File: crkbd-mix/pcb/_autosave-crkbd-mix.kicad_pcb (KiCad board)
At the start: 2 copper layers, 133.8 x 92.2 mm, 70 parts, among them J1 MJ-4PP-9, J2 OLED, P1 i2c-pin, P2 i2c-pin, SW1 SW_PUSH, SW10 SW_PUSH, SW11 SW_PUSH, SW12 SW_PUSH, SW13 SW_PUSH, SW14 SW_PUSH, SW15 SW_PUSH, SW16 SW_PUSH, SW17 SW_PUSH, SW18 SW_PUSH, SW19 SW_PUSH, SW2 SW_PUSH, SW20 SW_PUSH, SW21 SW_PUSH, SW3 SW_PUSH, SW4 SW_PUSH, SW5 SW_PUSH, SW6 SW_PUSH, SW7 SW_PUSH, SW8 SW_PUSH, SW9 SW_PUSH, U1 ProMicro

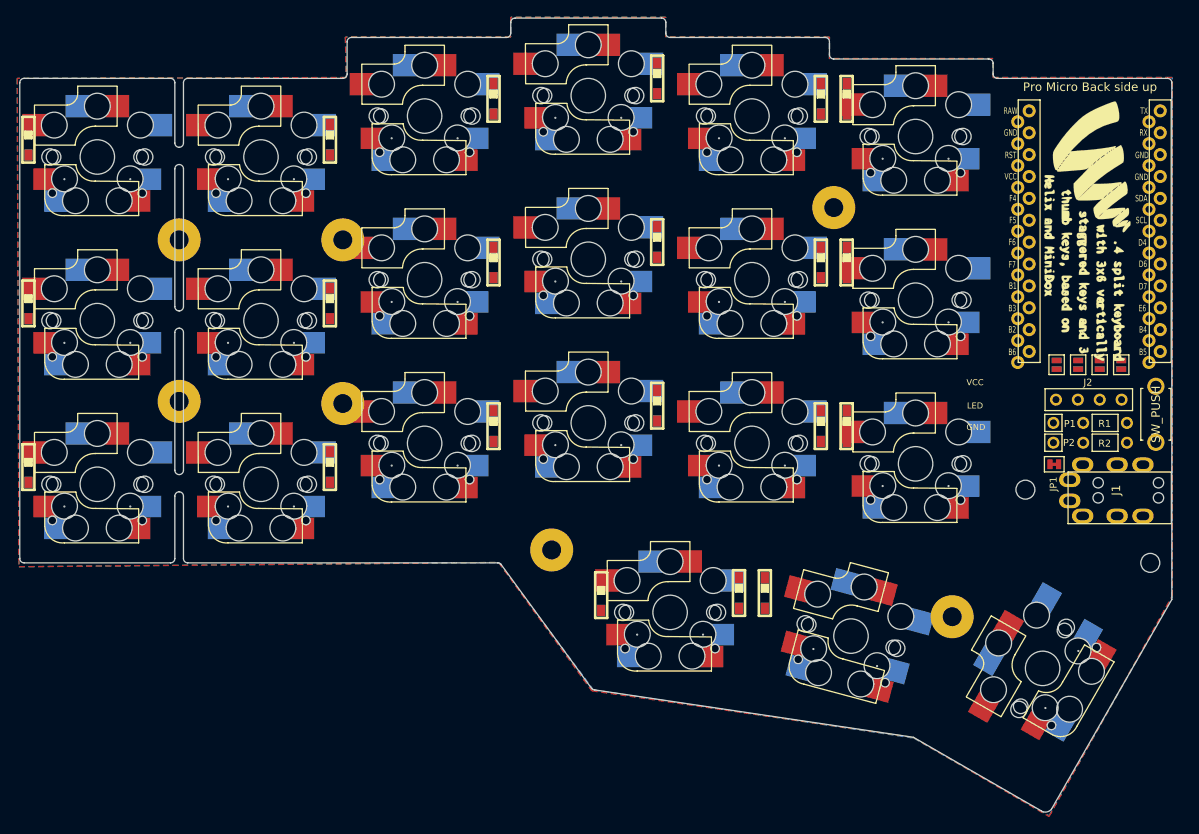
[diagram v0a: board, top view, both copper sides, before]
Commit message: Replace footprints for double hotswapable
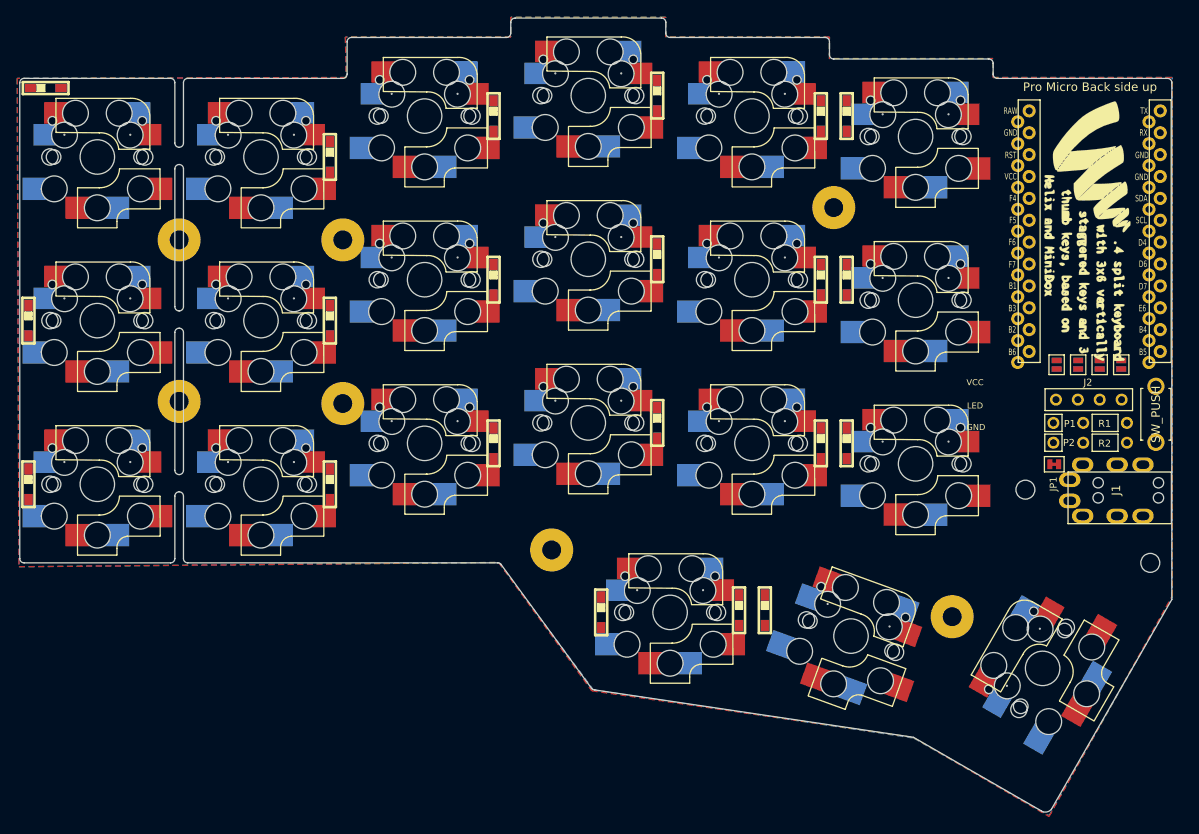
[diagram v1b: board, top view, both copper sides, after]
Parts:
- moved D1 6.32 mm to (64.0, 69.1), turned to 0 degrees
- moved D10 2.00 mm to (135.0, 89.0)
- moved D11 2.00 mm to (154.0, 91.4)
- moved D12 2.00 mm to (157.0, 91.4)
- moved D13 2.00 mm to (62.0, 115.1)
- moved D14 2.00 mm to (97.0, 115.1)
- moved D15 2.00 mm to (116.0, 110.4)
- moved D16 2.00 mm to (135.0, 108.0)
- moved D17 2.00 mm to (154.0, 110.4)
- moved D18 2.00 mm to (157.0, 110.4)
- moved D19 2.00 mm to (128.5, 130.0)
- moved D2 2.00 mm to (97.0, 77.1)
- moved D20 2.00 mm to (144.5, 129.8)
- moved D21 2.00 mm to (147.5, 129.8)
- moved D3 2.00 mm to (116.0, 72.4)
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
